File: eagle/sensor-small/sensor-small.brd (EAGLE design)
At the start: 33 x 25.4 mm, 13 parts, among them M1 NRF24-MODULE, U1 MSP430G2553IPW20, U3 SI7021, X1 1X05_1.27MM, X2 RENATA_SMTU2032-1

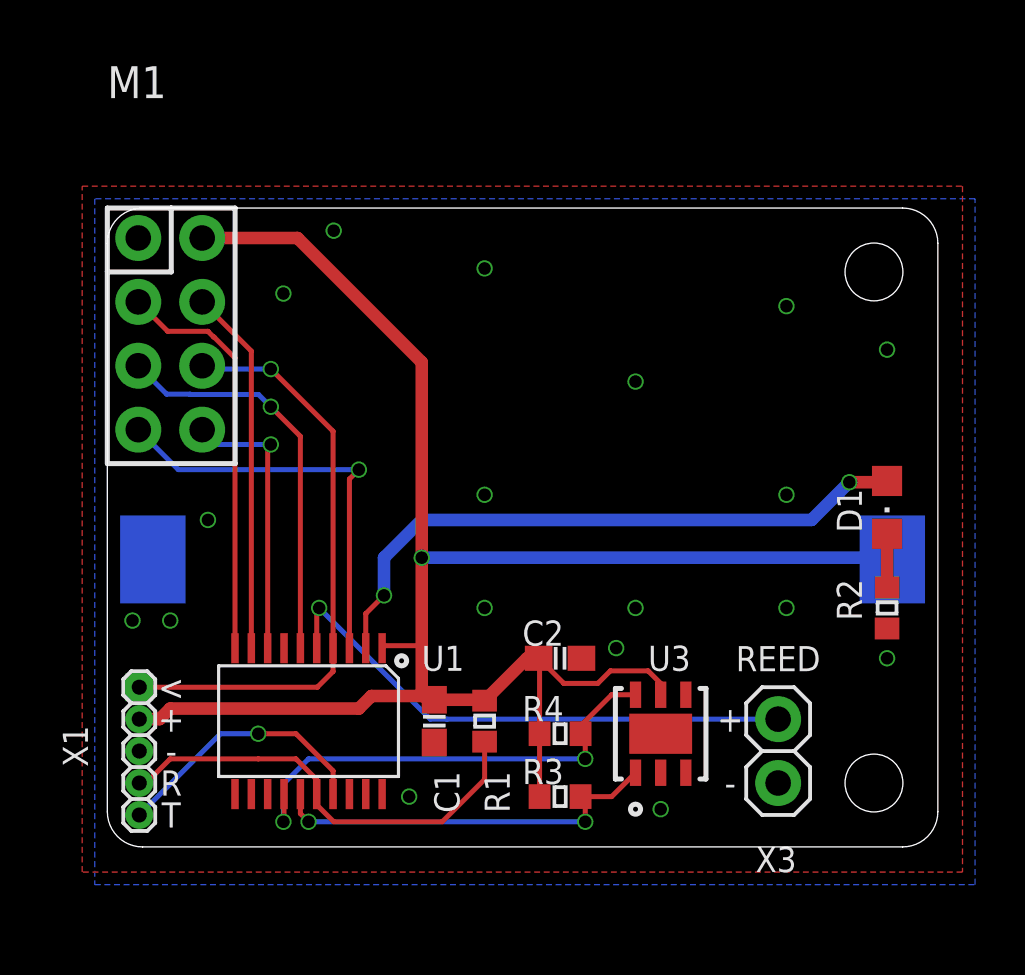
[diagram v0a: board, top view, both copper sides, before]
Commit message: Fixed swapped RST and TEST line in EAGLE design
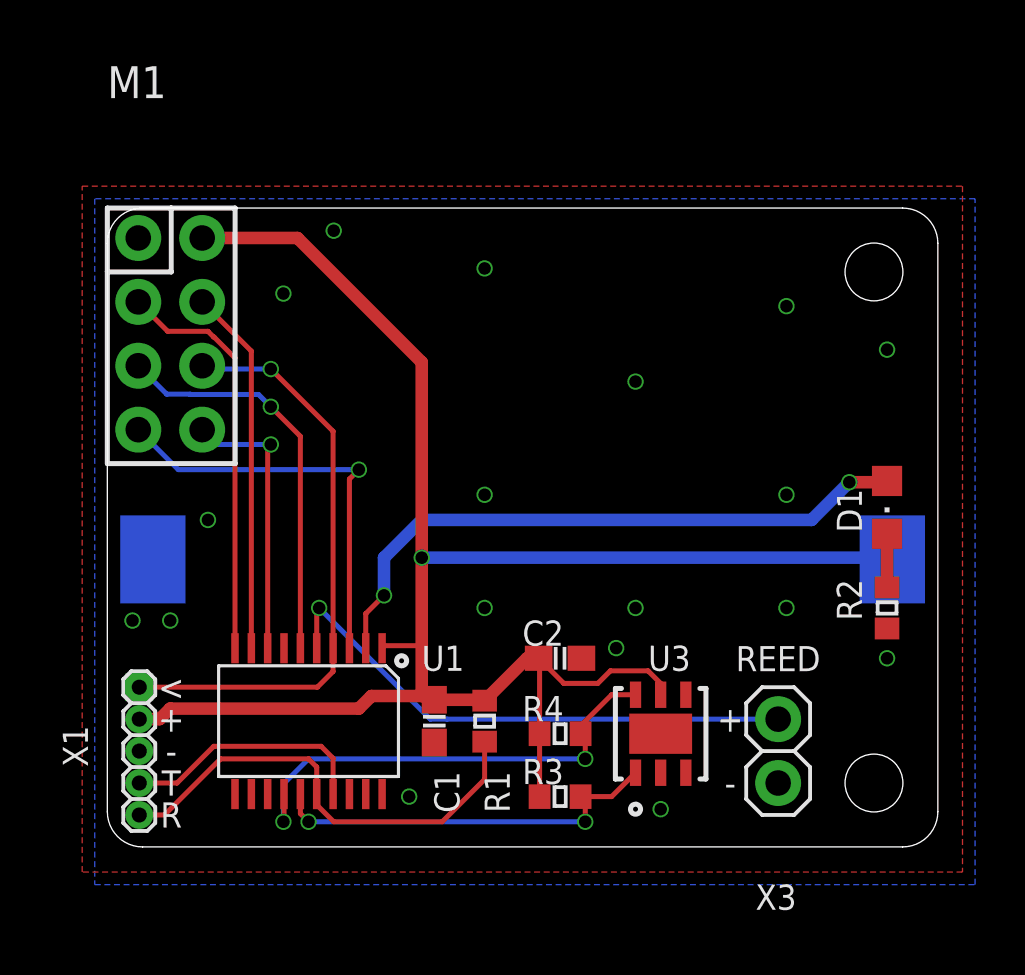
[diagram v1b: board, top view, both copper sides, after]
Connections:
- net N$2: now also X1.5; no longer X1.4
- net N$3: now also X1.4; no longer X1.5
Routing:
- net N$2: track 17.9 -> 18.8 mm
- net N$3: track 10.6 -> 9.93 mm, vias 1 -> 0
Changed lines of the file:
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@@
 <text x="2.54" y="5.08" size="1" layer="21" ratio="12" align="center">+</text>
 <text x="2.54" y="3.81" size="1" layer="21" ratio="12" align="center">-</text>
-<text x="2.54" y="2.54" size="1" layer="21" ratio="12" align="center">R</text>
-<text x="2.54" y="1.27" size="1" layer="21" ratio="12" align="center">T</text>
+<text x="2.54" y="1.27" size="1" layer="21" ratio="12" align="center">R</text>
+<text x="2.54" y="2.54" size="1" layer="21" ratio="12" align="center">T</text>
 <text x="27.23" y="24.27" size="1" layer="22" ratio="12" rot="MR0" align="center-left">MSP-NRF-WSN Sensor</text>
 <text x="27.23" y="22.77" size="1" layer="22" ratio="12" rot="MR0" align="center-left">RFr 2022-02</text>
@@
 </element>
 <element name="X3" library="rfr-lib-connector" package="1X02" value="" x="26.67" y="3.81" smashed="yes" rot="R270">
-<attribute name="NAME" x="25.77" y="-1" size="1" layer="25" ratio="12"/>
+<attribute name="NAME" x="25.77" y="-2.5" size="1" layer="25" ratio="12"/>
 <attribute name="VALUE" x="28.67" y="5.81" size="1" layer="27" ratio="12" rot="R270"/>
 </element>
@@
 <wire x1="17.185" y1="4.5" x2="17.185" y2="7.465" width="0.2" layer="1"/>
 <wire x1="17.185" y1="7.465" x2="17.15" y2="7.5" width="0.2" layer="1"/>
-<wire x1="17.15" y1="7.5" x2="17.15" y2="7.65" width="0.2" layer="1"/>
 <wire x1="31.21" y1="11.43" x2="31.14" y2="11.5" width="0.5" layer="16"/>
 <wire x1="31.14" y1="11.5" x2="12.5" y2="11.5" width="0.5" layer="16"/>
@@
 <contactref element="U1" pad="16"/>
 <contactref element="R1" pad="1"/>
-<contactref element="X1" pad="4"/>
-<wire x1="1.27" y1="2.54" x2="1.54" y2="2.54" width="0.2" layer="1"/>
-<wire x1="1.54" y1="2.54" x2="2.5" y2="3.5" width="0.2" layer="1"/>
-<wire x1="2.5" y1="3.5" x2="6" y2="3.5" width="0.2" layer="1"/>
-<wire x1="6" y1="3.5" x2="7.5" y2="3.5" width="0.2" layer="1"/>
-<wire x1="8.325" y1="2.1" x2="8.325" y2="2.675" width="0.2" layer="1"/>
-<wire x1="8.325" y1="2.675" x2="7.5" y2="3.5" width="0.2" layer="1"/>
 <wire x1="8.325" y1="2.1" x2="8.325" y2="1.675" width="0.2" layer="1"/>
 <wire x1="8.325" y1="1.675" x2="9" y2="1" width="0.2" layer="1"/>
@@
 <wire x1="15" y1="2.685" x2="15" y2="4.185" width="0.2" layer="1"/>
 <wire x1="9" y1="1" x2="13.315" y2="1" width="0.2" layer="1"/>
-</signal>
-<signal name="N$3">
-<contactref element="U1" pad="17"/>
 <contactref element="X1" pad="5"/>
-<wire x1="8.975" y1="2.1" x2="8.975" y2="3.025" width="0.2" layer="1"/>
-<wire x1="7.5" y1="4.5" x2="6" y2="4.5" width="0.2" layer="1"/>
-<via x="6" y="4.5" extent="1-16" drill="0.5"/>
-<wire x1="8.975" y1="3.025" x2="7.5" y2="4.5" width="0.2" layer="1"/>
-<wire x1="6" y1="4.5" x2="4.5" y2="4.5" width="0.2" layer="16"/>
-<wire x1="4.5" y1="4.5" x2="1.27" y2="1.27" width="0.2" layer="16"/>
+<wire x1="8.325" y1="2.1" x2="8.325" y2="3.175" width="0.2" layer="1"/>
+<wire x1="8.325" y1="3.175" x2="8" y2="3.5" width="0.2" layer="1"/>
+<wire x1="8" y1="3.5" x2="4.5" y2="3.5" width="0.2" layer="1"/>
+<wire x1="4.5" y1="3.5" x2="2.27" y2="1.27" width="0.2" layer="1"/>
+<wire x1="2.27" y1="1.27" x2="1.27" y2="1.27" width="0.2" layer="1"/>
 </signal>
 <signal name="P_SCK">
@@
 <wire x1="31" y1="12.45" x2="31" y2="10.315" width="0.5" layer="1"/>
 </signal>
+<signal name="N$3">
+<contactref element="X1" pad="4"/>
+<contactref element="U1" pad="17"/>
+<wire x1="8.975" y1="2.1" x2="8.975" y2="3.525" width="0.2" layer="1"/>
+<wire x1="8.975" y1="3.525" x2="8.5" y2="4" width="0.2" layer="1"/>
+<wire x1="4.23" y1="4" x2="2.77" y2="2.54" width="0.2" layer="1"/>
+<wire x1="2.77" y1="2.54" x2="1.27" y2="2.54" width="0.2" layer="1"/>
+<wire x1="8.5" y1="4" x2="4.23" y2="4" width="0.2" layer="1"/>
+</signal>
 </signals>

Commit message: Changed LED resistor value
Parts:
- R2: value 470k -> 470
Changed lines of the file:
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@@
 <attribute name="VALUE" x="13.2" y="3.5" size="1" layer="27" ratio="12" rot="R90"/>
 </element>
-<element name="R2" library="rfr-lib-passive" package="R0603" value="470k" x="31" y="9.5" smashed="yes" rot="R270">
+<element name="R2" library="rfr-lib-passive" package="R0603" value="470" x="31" y="9.5" smashed="yes" rot="R270">
 <attribute name="NAME" x="30" y="9" size="1" layer="25" ratio="12" rot="R90"/>
 <attribute name="VALUE" x="32.8" y="11" size="1" layer="27" ratio="12" rot="R270"/>
